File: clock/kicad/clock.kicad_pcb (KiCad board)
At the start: 2 copper layers, 147.3 x 68.6 mm, 79 parts, among them SW1 HOUR, SW2 MIN, SW3 TIME, U1 74HC4060, U10 74HC4511, U11 74HC4511, U12 74HC4511, U13 74HC4511, U14 KCSC02-105, U15 KCSC02-105, U16 KCSC02-105, U17 KCSC02-105, U18 KCSC02-105, U19 KCSC02-105, U2 SN74HC74N, U20 74HC14, U21 74HC157, U3 74HC390, U4 74HC08, U5 74HC390, U6 74HC08, U7 74HC390, U8 74HC4511, U9 74HC4511

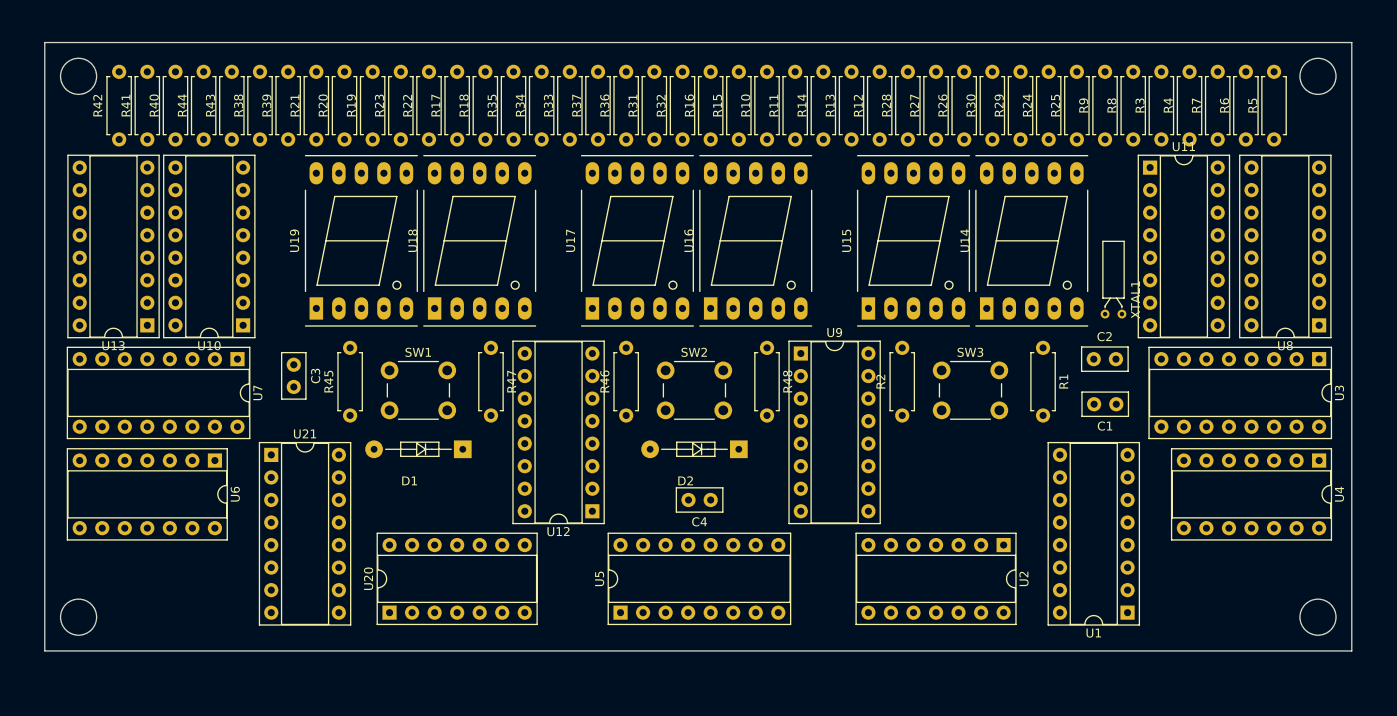
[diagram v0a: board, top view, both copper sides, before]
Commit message: Clock: Created PCB Layout.
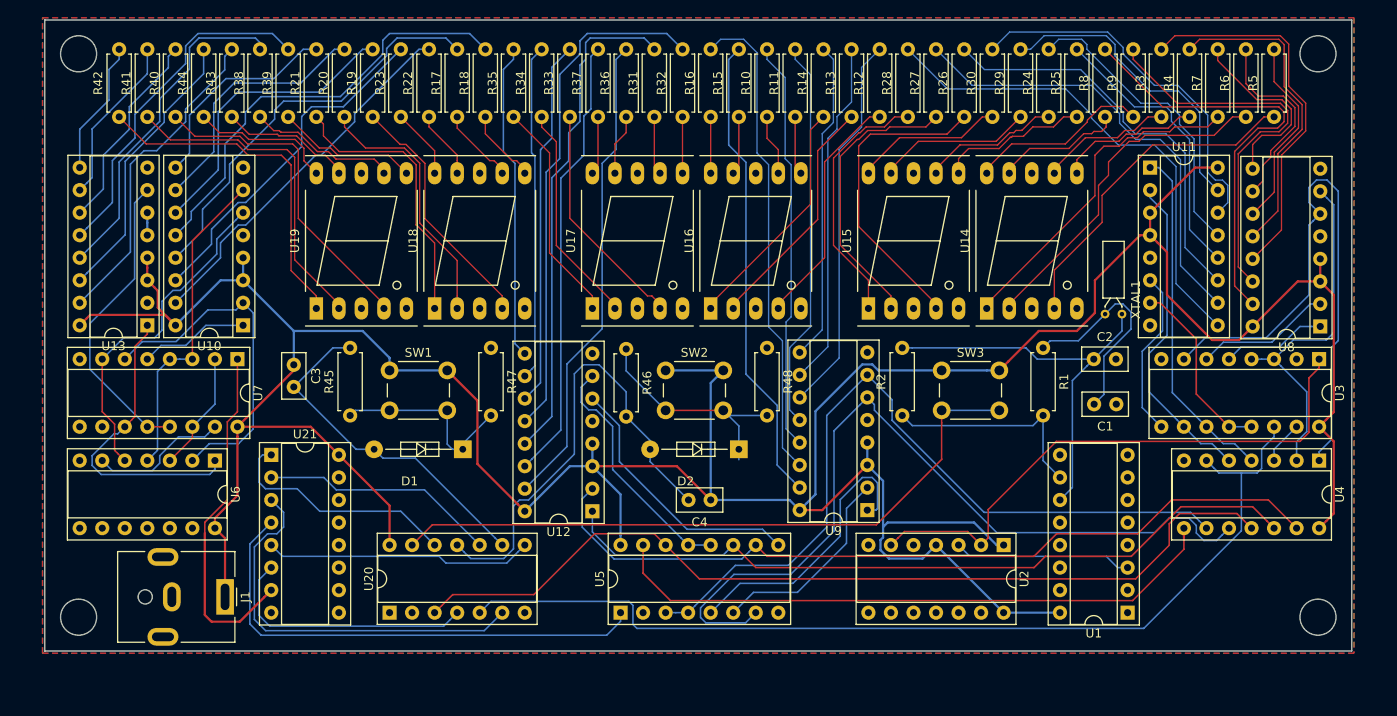
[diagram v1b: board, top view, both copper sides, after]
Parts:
- added J1: Jack-DC, KiCad:BarrelJack_CUI_PJ-063AH_Horizontal, F.Cu at (147.3, 120.9)
- moved U9 19.2 mm to (219.7, 111.1), turned to 180 degrees
- moved R46 7.49 mm to (192.5, 93.0), turned to 270 degrees
- moved R8 4.07 mm to (246.5, 66.8)
- moved R9 4.07 mm to (249.7, 66.8)
- moved R10 2.54 mm to (208.4, 66.8)
- moved R11 2.54 mm to (211.6, 66.8)
- moved R12 2.54 mm to (221.1, 66.8)
- moved R13 2.54 mm to (217.9, 66.8)
- moved R14 2.54 mm to (214.8, 66.8)
- moved R15 2.54 mm to (205.2, 66.8)
- moved R16 2.54 mm to (202.1, 66.8)
- moved R17 2.54 mm to (173.5, 66.8)
- moved R18 2.54 mm to (176.7, 66.8)
- moved R19 2.54 mm to (164.0, 66.8)
- moved R20 2.54 mm to (160.8, 66.8)
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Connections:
- U21 pad 10: (no net) -> GND
- U21 pad 3: GND -> Net-(U20-Pad6)
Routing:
- net VCC: track 0.00 -> 406.9 mm
- net Net-(U20-Pad5): track 0.00 -> 112.3 mm
- net Net-(U20-Pad3): track 0.00 -> 103.0 mm
- net Net-(U4-Pad10): track 0.00 -> 93.5 mm
- net Net-(U12-Pad2): track 0.00 -> 91.9 mm
- net Net-(U4-Pad9): track 0.00 -> 87.9 mm
- net Net-(U12-Pad1): track 0.00 -> 85.6 mm
- net Net-(SW3-Pad2): track 0.00 -> 75.7 mm
- net Net-(U4-Pad8): track 0.00 -> 70.2 mm
- net Net-(U3-Pad7): track 0.00 -> 65.7 mm
- net Net-(U2-Pad2): track 0.00 -> 64.2 mm
- net Net-(R32-Pad2): track 0.00 -> 58.1 mm
- net Net-(R31-Pad2): track 0.00 -> 56.6 mm
- net Net-(U21-Pad4): track 0.00 -> 56.4 mm
- net Net-(R28-Pad2): track 0.00 -> 55.8 mm
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- added copper zone on B.Cu, net GND
- added copper zone on F.Cu, net GND
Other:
- board size 147.3 x 68.6 mm -> 147.3 x 71.1 mm

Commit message: Clock: Add Gerber files
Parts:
- moved J1 5.59 mm to (141.7, 120.9)
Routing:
- net Net-(U21-Pad7): track 39.6 -> 31.5 mm
- net VCC: track 406.9 -> 409.0 mm
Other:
- outline, holes or cut-outs redrawn
- board text added: "24H DIGITAL CLOCK ERIK VAN ZIJST, 2019"
- board text added: "HOUR"
- board text added: "MINUTE"
- board text added: "SET TIME"
- board text added: "v01"

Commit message: Clock: Added Decoupling Capacitors.
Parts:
- added C10: 100nF, Capacitor_THT:C_Disc_D5.0mm_W2.5mm_P2.50mm, F.Cu at (273.8, 99.3)
- added C11: 100nF, Capacitor_THT:C_Disc_D5.0mm_W2.5mm_P2.50mm, F.Cu at (273.8, 110.7)
- added C12: 100nF, Capacitor_THT:C_Disc_D5.0mm_W2.5mm_P2.50mm, F.Cu at (188.5, 115.1)
- added C13: 100nF, Capacitor_THT:C_Disc_D5.0mm_W2.5mm_P2.50mm, F.Cu at (149.4, 113.3)
- added C14: 100nF, Capacitor_THT:C_Disc_D5.0mm_W2.5mm_P2.50mm, F.Cu at (262.6, 90.4)
- added C15: 100nF, Capacitor_THT:C_Disc_D5.0mm_W2.5mm_P2.50mm, F.Cu at (208.8, 111.3)
- added C16: 100nF, Capacitor_THT:C_Disc_D5.0mm_W2.5mm_P2.50mm, F.Cu at (138.4, 90.4)
- added C17: 100nF, Capacitor_THT:C_Disc_D5.0mm_W2.5mm_P2.50mm, F.Cu at (262.4, 72.4)
- added C18: 100nF, Capacitor_THT:C_Disc_D5.0mm_W2.5mm_P2.50mm, F.Cu at (177.8, 111.3)
- added C19: 100nF, Capacitor_THT:C_Disc_D5.0mm_W2.5mm_P2.50mm, F.Cu at (127.5, 94.0)
- added C5: 100nF, Capacitor_THT:C_Disc_D5.0mm_W2.5mm_P2.50mm, F.Cu at (238.3, 122.7)
- added C6: 100nF, Capacitor_THT:C_Disc_D5.0mm_W2.5mm_P2.50mm, F.Cu at (165.9, 111.8)
- added C8: 100nF, Capacitor_THT:C_Disc_D5.0mm_W2.5mm_P2.50mm, F.Cu at (163.3, 107.2)
- added C9: 100nF, Capacitor_THT:C_Disc_D5.0mm_W2.5mm_P2.50mm, F.Cu at (149.4, 107.4)
- moved U13 3.56 mm to (135.0, 90.3)
- moved J1 2.79 mm to (138.9, 120.9)
- moved U8 2.79 mm to (273.6, 90.4)
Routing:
- net VCC: track 409.0 -> 430.6 mm
- net Net-(R3-Pad2): track 42.9 -> 37.6 mm
- net Net-(R39-Pad2): track 39.2 -> 44.4 mm
- net Net-(R44-Pad2): track 31.8 -> 36.0 mm
- net Net-(R40-Pad2): track 22.9 -> 27.0 mm
- net Net-(U3-Pad3): track 40.5 -> 44.6 mm
- net Net-(R38-Pad2): track 38.2 -> 42.1 mm
- net Net-(R43-Pad2): track 36.5 -> 40.1 mm
- net Net-(U3-Pad7): track 65.7 -> 68.9 mm
- net Net-(R41-Pad2): track 19.0 -> 22.2 mm
- net Net-(U3-Pad6): track 15.4 -> 18.3 mm
- net Net-(U3-Pad5): track 11.8 -> 14.6 mm
- net GND: track 2.54 -> 0.00 mm
- net Net-(U5-Pad5): track 31.9 -> 34.4 mm
- net Net-(U5-Pad6): track 23.3 -> 25.6 mm
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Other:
- board size 147.3 x 71.1 mm -> 152.9 x 71.1 mm

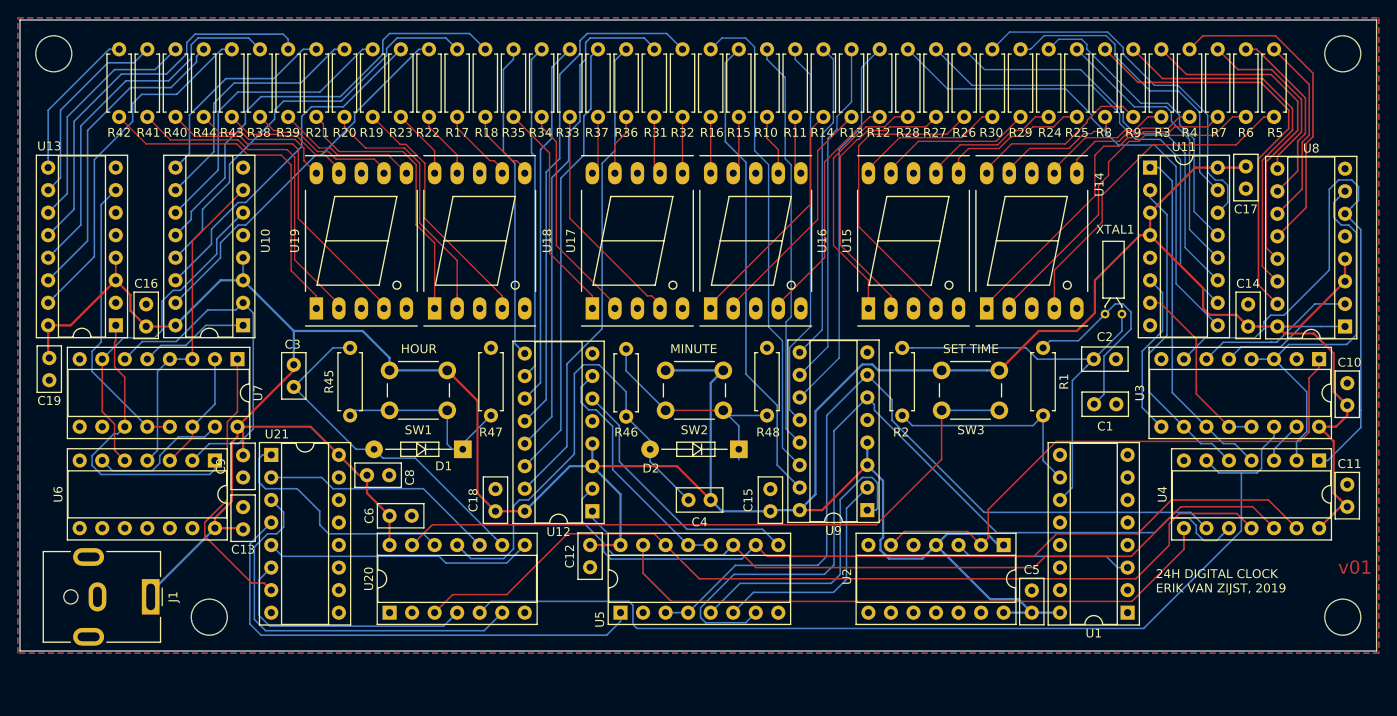
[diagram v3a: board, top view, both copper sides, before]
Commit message: Clock: Added USB power connector.
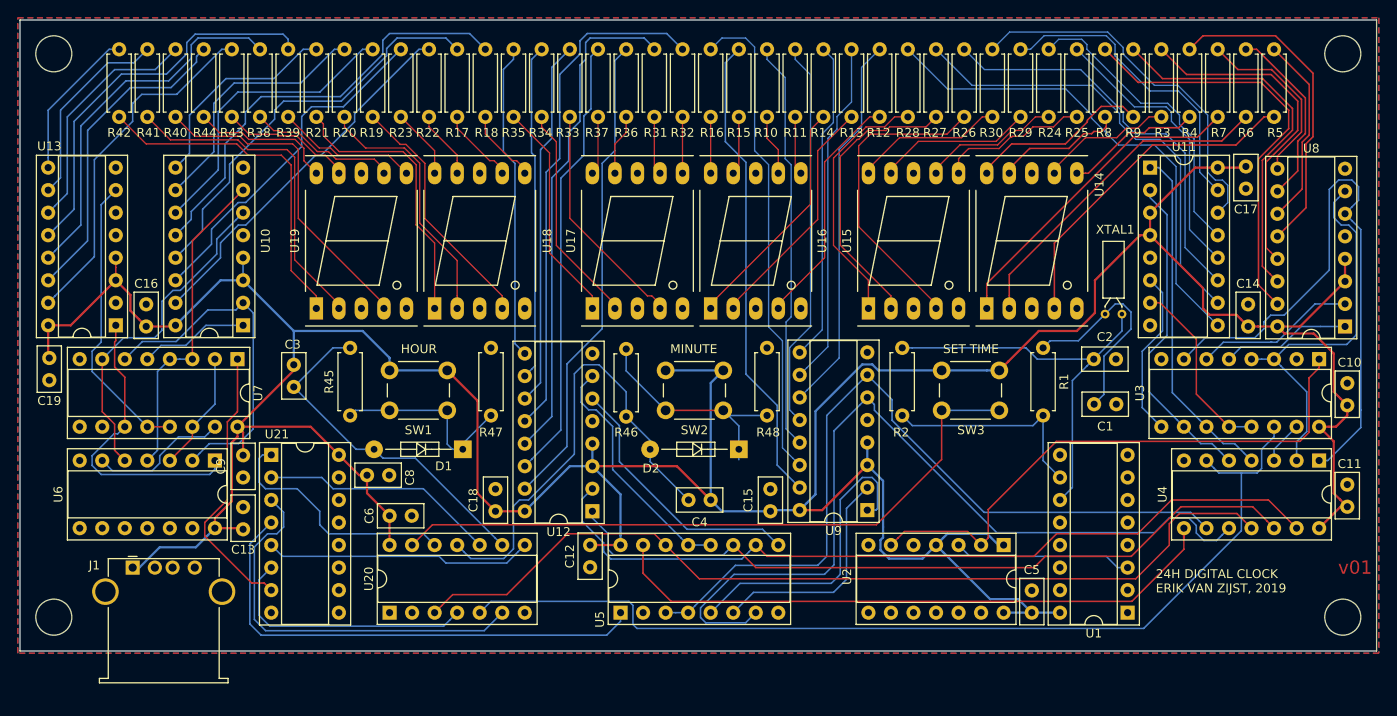
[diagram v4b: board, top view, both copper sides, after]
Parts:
- J1: value Jack-DC -> USB-SS-52100-001; footprint KiCad:BarrelJack_CUI_PJ-063AH_Horizontal -> KiCad:USB_A_Stewart_SS-52100-001_Horizontal
- moved J1 3.88 mm to (136.9, 117.6), turned to 0 degrees
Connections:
- J1 pad 2: GND -> Net-(J1-Pad2)
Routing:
- net Net-(R7-Pad1): track 38.0 -> 36.6 mm
- net Net-(R4-Pad1): track 16.2 -> 15.3 mm
- net Net-(R6-Pad1): track 38.7 -> 37.8 mm
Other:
- outline, holes or cut-outs redrawn

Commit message: Clock: Added decoupling capacitor to 74hc74 flip flop.
Also added fifth mounting hole in the middle of the board.
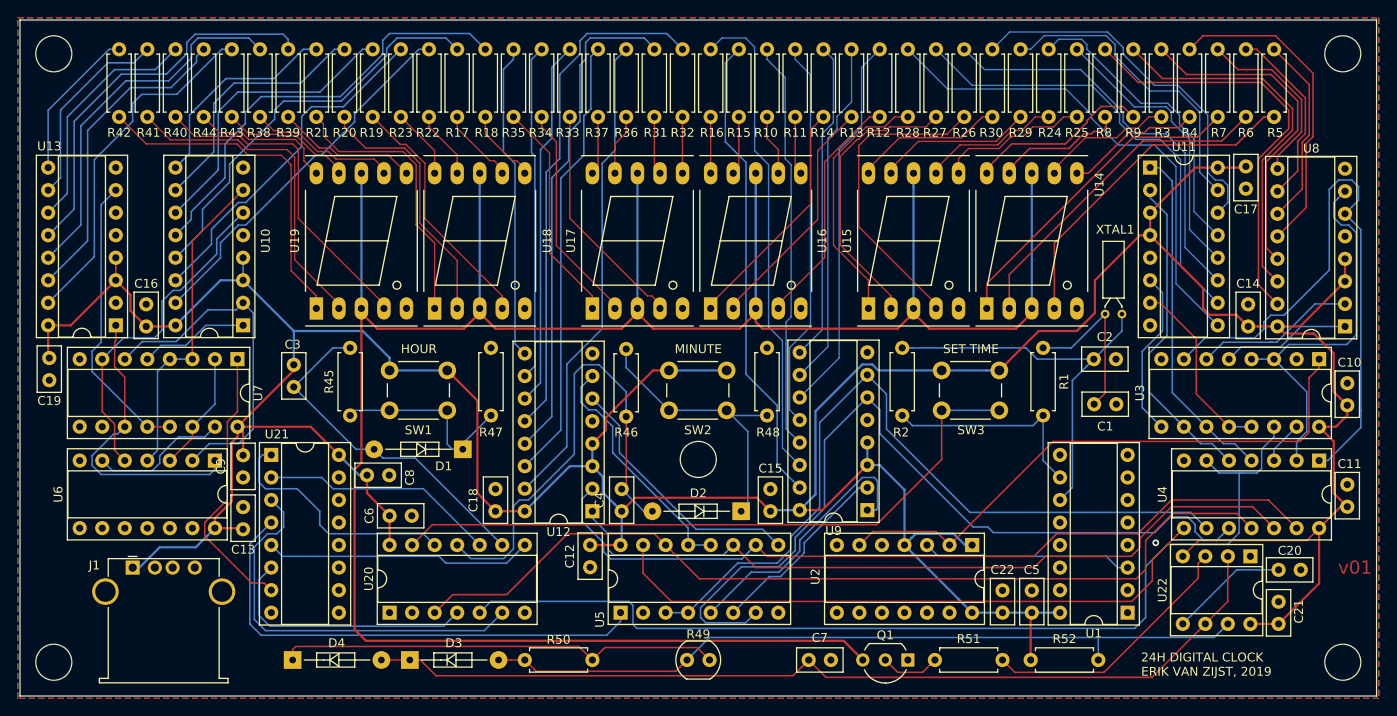
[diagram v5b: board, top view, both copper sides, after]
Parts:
- added C20: 10nF, Capacitor_THT:C_Disc_D5.0mm_W2.5mm_P2.50mm, F.Cu at (266.1, 117.9)
- added C21: 100nF, Capacitor_THT:C_Disc_D5.0mm_W2.5mm_P2.50mm, F.Cu at (266.1, 124.0)
- added C22: 100nF, Capacitor_THT:C_Disc_D5.0mm_W2.5mm_P2.50mm, F.Cu at (234.9, 122.7)
- added C7: 100nF, Capacitor_THT:C_Disc_D5.0mm_W2.5mm_P2.50mm, F.Cu at (213.1, 128.0)
- added D3: D, digikey-footprints:Diode_DO-35_P10mm, F.Cu at (168.1, 128.0)
- added D4: D, digikey-footprints:Diode_DO-35_P10mm, F.Cu at (154.9, 128.0)
- added Q1: PN2222A, Package_TO_SOT_THT:TO-92_Inline_Wide, F.Cu at (224.3, 128.0)
- added R49: VT93xx, OptoDevice:R_LDR_4.9x4.2mm_P2.54mm_Vertical, F.Cu at (199.4, 128.0)
- added R50: 100K, Resistor_THT:R_Axial_DIN0207_L6.3mm_D2.5mm_P7.62mm_Horizontal, F.Cu at (188.7, 128.0)
- added R51: 100K, Resistor_THT:R_Axial_DIN0207_L6.3mm_D2.5mm_P7.62mm_Horizontal, F.Cu at (227.3, 128.0)
- added R52: 1K, Resistor_THT:R_Axial_DIN0207_L6.3mm_D2.5mm_P7.62mm_Horizontal, F.Cu at (238.1, 128.0)
- added U22: NE555P, Package_DIP:DIP-8_W7.62mm_Socket, F.Cu at (262.9, 116.3)
- moved C4 10.1 mm to (192.0, 111.3), turned to 90 degrees
- moved D2 6.99 mm to (205.5, 111.3)
- moved U2 3.56 mm to (231.5, 115.1)
- moved SW2 0.38 mm to (197.4, 95.4)
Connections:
- U14 pad 3: GND -> Net-(Q1-Pad3)
- U14 pad 8: GND -> Net-(Q1-Pad3)
- U15 pad 3: GND -> Net-(Q1-Pad3)
- U15 pad 8: GND -> Net-(Q1-Pad3)
- U16 pad 3: GND -> Net-(Q1-Pad3)
- U16 pad 8: GND -> Net-(Q1-Pad3)
- U17 pad 3: GND -> Net-(Q1-Pad3)
- U17 pad 8: GND -> Net-(Q1-Pad3)
- U18 pad 3: GND -> Net-(Q1-Pad3)
- U18 pad 8: GND -> Net-(Q1-Pad3)
- U19 pad 3: GND -> Net-(Q1-Pad3)
- U19 pad 8: GND -> Net-(Q1-Pad3)
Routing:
- net Net-(Q1-Pad3): track 0.00 -> 274.2 mm
- net Net-(C7-Pad1): track 0.00 -> 106.3 mm
- net Net-(D3-Pad2): track 0.00 -> 87.5 mm
- net Net-(D4-Pad1): track 0.00 -> 50.1 mm
- net Net-(R51-Pad2): track 0.00 -> 29.8 mm
- net VCC: track 431.0 -> 456.7 mm
- net Net-(C20-Pad1): track 0.00 -> 13.3 mm
- net Net-(Q1-Pad2): track 0.00 -> 6.75 mm
- net Net-(D2-Pad1): track 26.7 -> 33.1 mm
- net Net-(C1-Pad2): track 24.4 -> 19.2 mm
- net Net-(U5-Pad5): track 34.4 -> 30.4 mm
- net Net-(U5-Pad6): track 25.6 -> 21.6 mm
- net Net-(U1-Pad3): track 20.1 -> 23.7 mm
- net Net-(U20-Pad5): track 112.3 -> 115.5 mm
- net Net-(U2-Pad2): track 64.2 -> 67.1 mm
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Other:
- board size 152.9 x 71.1 mm -> 152.9 x 76.2 mm
- rule solder_mask_min_width: 0.25 -> 0.1778
- board text added: "github.com/erikvanzijst/clock"

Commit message: Clock: Isolated Crystal Circuit.
Also removed the gap between the 7-segment displays of each cluster.
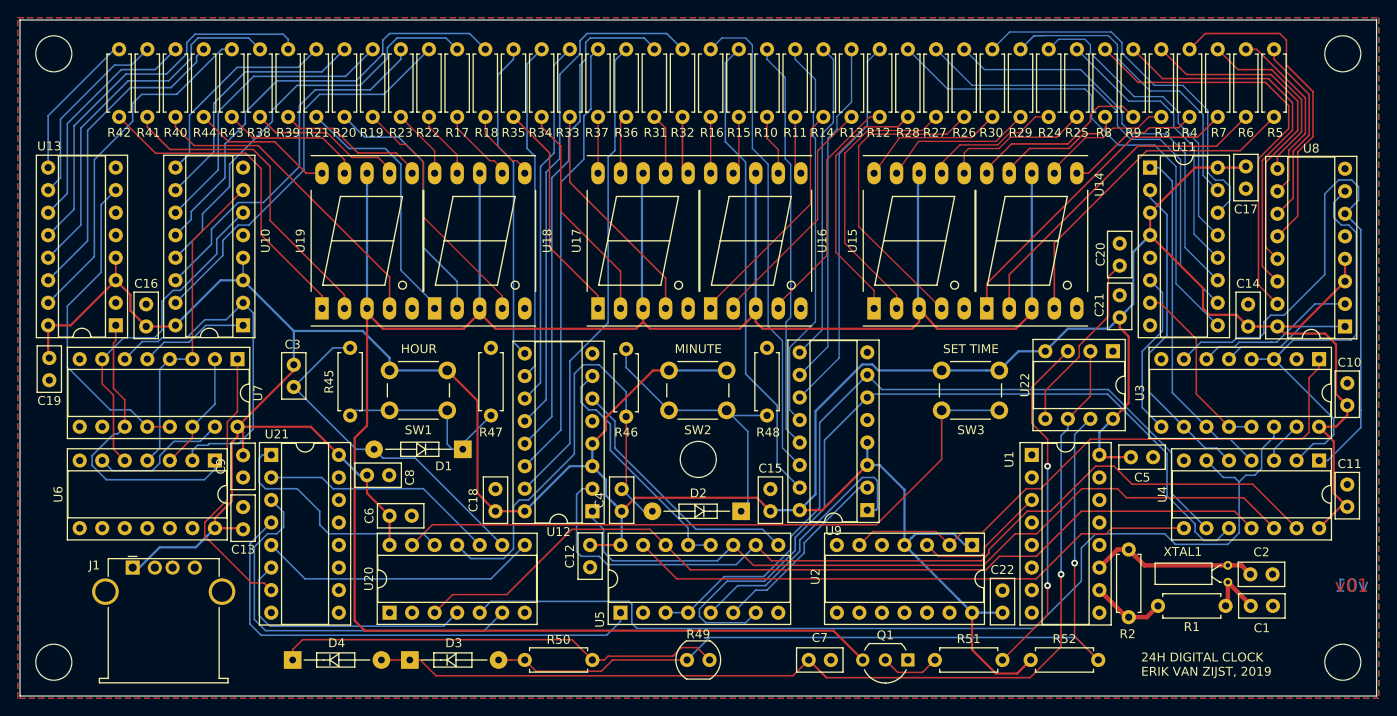
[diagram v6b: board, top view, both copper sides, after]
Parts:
- moved C21 38.9 mm to (248.2, 89.4)
- moved C20 38.7 mm to (248.2, 83.6), turned to 90 degrees
- moved R1 35.6 mm to (260.1, 121.9), turned to 180 degrees
- moved R2 34.2 mm to (249.2, 123.2)
- moved XTAL1 30.7 mm to (260.4, 117.3), turned to 270 degrees
- moved C2 30.0 mm to (262.9, 118.4)
- moved C1 28.8 mm to (265.4, 121.9)
- moved U22 27.8 mm to (247.4, 93.2)
- moved U1 20.8 mm to (238.3, 104.9), turned to 0 degrees
- moved C5 20.8 mm to (249.4, 105.2), turned to 0 degrees
- moved U15 0.64 mm to (220.5, 88.4)
- moved U17 0.63 mm to (189.4, 88.4)
- moved U19 0.63 mm to (158.2, 88.4)
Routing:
- net Net-(C2-Pad1): track 46.0 -> 19.0 mm
- net Net-(R1-Pad2): track 24.6 -> 8.39 mm
- net Net-(C1-Pad2): track 19.2 -> 6.61 mm
- net Net-(D3-Pad2): track 87.5 -> 99.8 mm, vias 0 -> 1
- net Net-(C7-Pad1): track 106.3 -> 117.8 mm, vias 0 -> 1
- net Net-(R51-Pad2): track 29.8 -> 39.3 mm, vias 0 -> 2
- net VCC: track 456.7 -> 447.9 mm
- net Net-(U1-Pad3): track 23.7 -> 15.3 mm
- net Net-(C20-Pad1): track 13.3 -> 20.7 mm
- net Net-(U12-Pad2): track 92.2 -> 99.5 mm
- net Net-(U4-Pad8): track 70.3 -> 64.9 mm
- net Net-(U13-Pad7): track 32.9 -> 36.5 mm
- net Net-(R22-Pad2): track 41.9 -> 45.4 mm
- net Net-(U3-Pad3): track 44.6 -> 47.9 mm
- net Net-(R23-Pad2): track 39.2 -> 41.9 mm
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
